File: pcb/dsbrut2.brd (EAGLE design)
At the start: 100 x 80 mm, 11 parts, among them IC1 4175D, IC2 74HC125D, IC3 MEGA8-AI

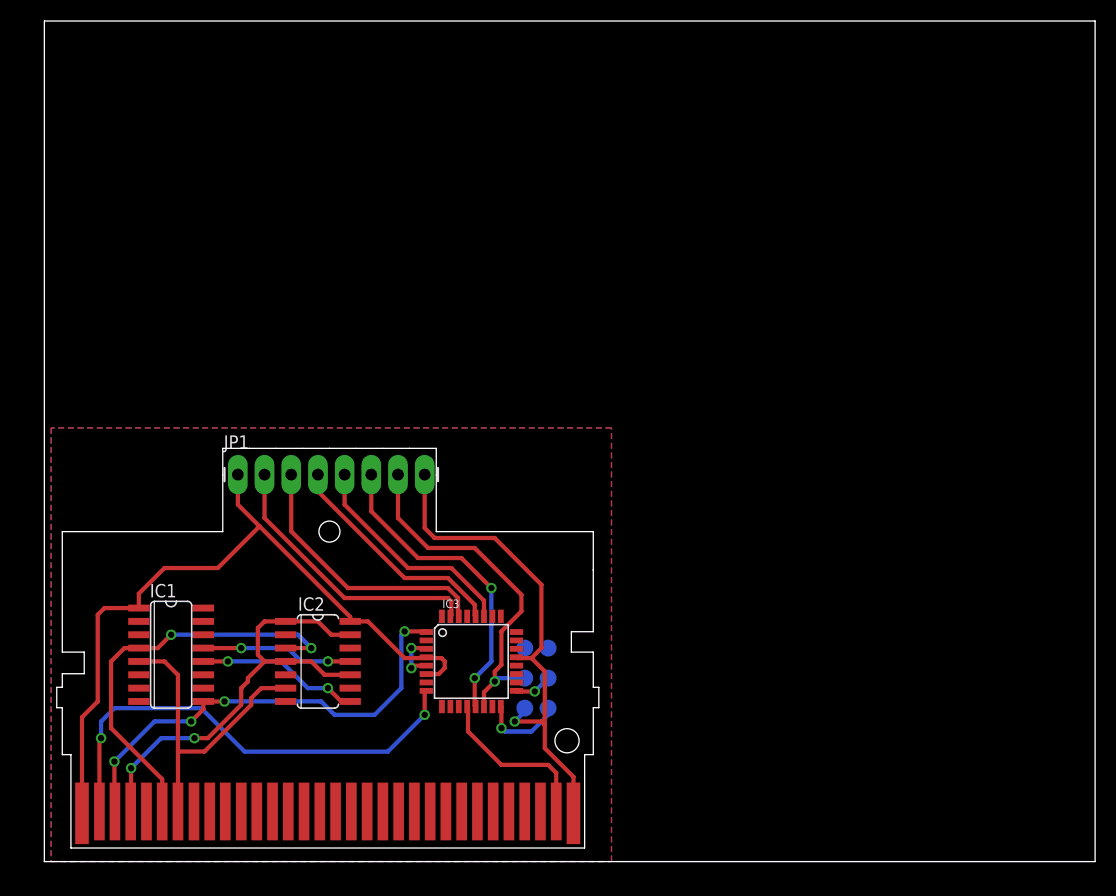
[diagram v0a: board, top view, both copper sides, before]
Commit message: updated isp progheader - please verify orientation
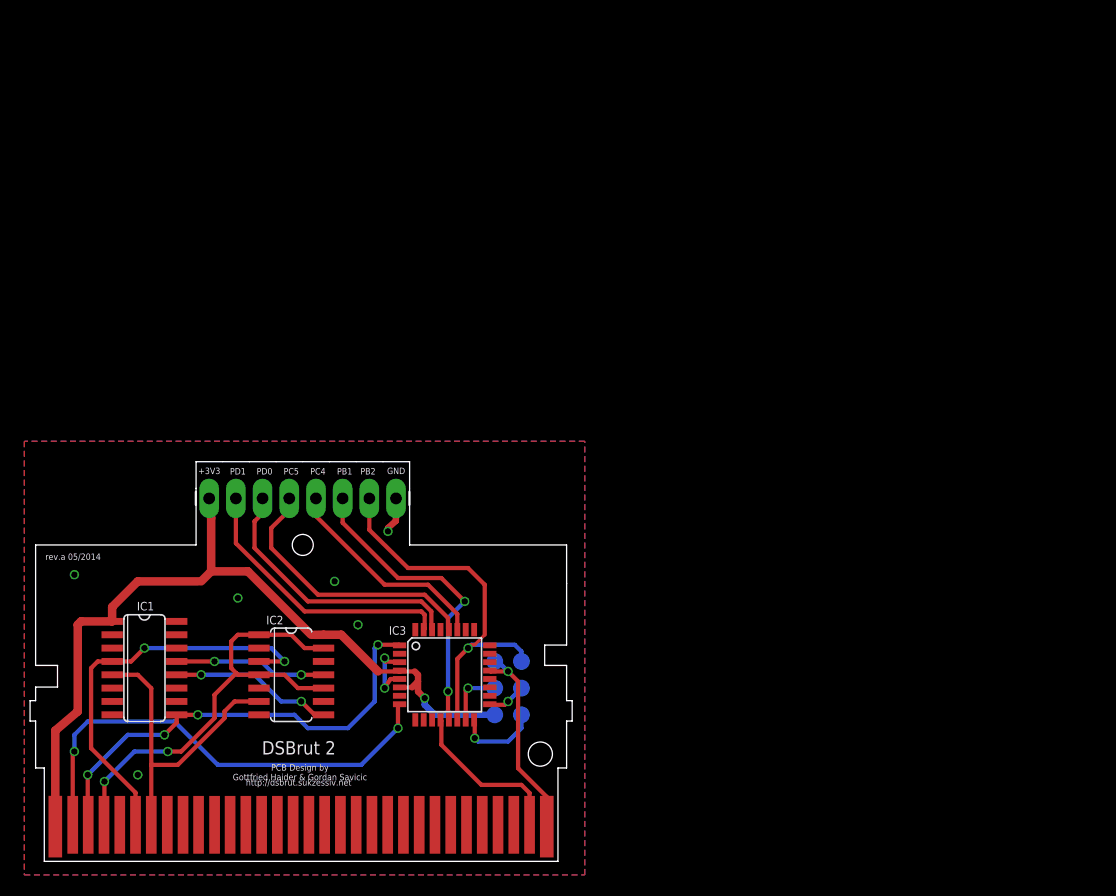
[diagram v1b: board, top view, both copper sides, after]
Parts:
- moved TP1 6.96 mm to (42.9, 14.0)
- moved TP2 6.35 mm to (42.9, 16.5)
- moved TP6 5.28 mm to (42.9, 19.1)
- moved JP1 3.54 mm to (15.7, 34.6)
- moved U$1 2.84 mm to (0.00, 0.00)
- moved IC1 2.84 mm to (9.53, 18.4)
- moved IC2 2.84 mm to (23.5, 17.8)
- moved IC3 2.84 mm to (38.1, 17.8)
- moved TP4 2.71 mm to (45.4, 16.5)
- moved TP3 2.62 mm to (45.4, 14.0)
- moved TP5 1.62 mm to (45.4, 19.1)
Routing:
- net GND: track 53.2 -> 29.6 mm, vias 3 -> 9
- net +3V3: track 70.9 -> 78.8 mm, vias 0 -> 1
- net MOSI: track 0.00 -> 5.65 mm, vias 0 -> 1
- net PC5: track 22.1 -> 26.2 mm
- net PB2: track 34.0 -> 36.7 mm
- net PB1: track 29.9 -> 29.0 mm
- net PC4: track 21.4 -> 20.5 mm
- net GBA6: track 39.4 -> 38.8 mm
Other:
- board size 100 x 80 mm -> 51.6 x 38 mm
- board text added: "+3V3"
- board text added: "DSBrut 2"
- board text added: "GND"
- board text added: "PB1"
- board text added: "PB2"
- board text added: "PC4"
- board text added: "PC5"
- board text added: "PCB Design by Gottfried Haider & Gordan Savicic"
- board text added: "PD0"
- board text added: "PD1"
- board text added: "http://dsbrut.sukzessiv.net"
- board text added: "rev.a 05/2014"

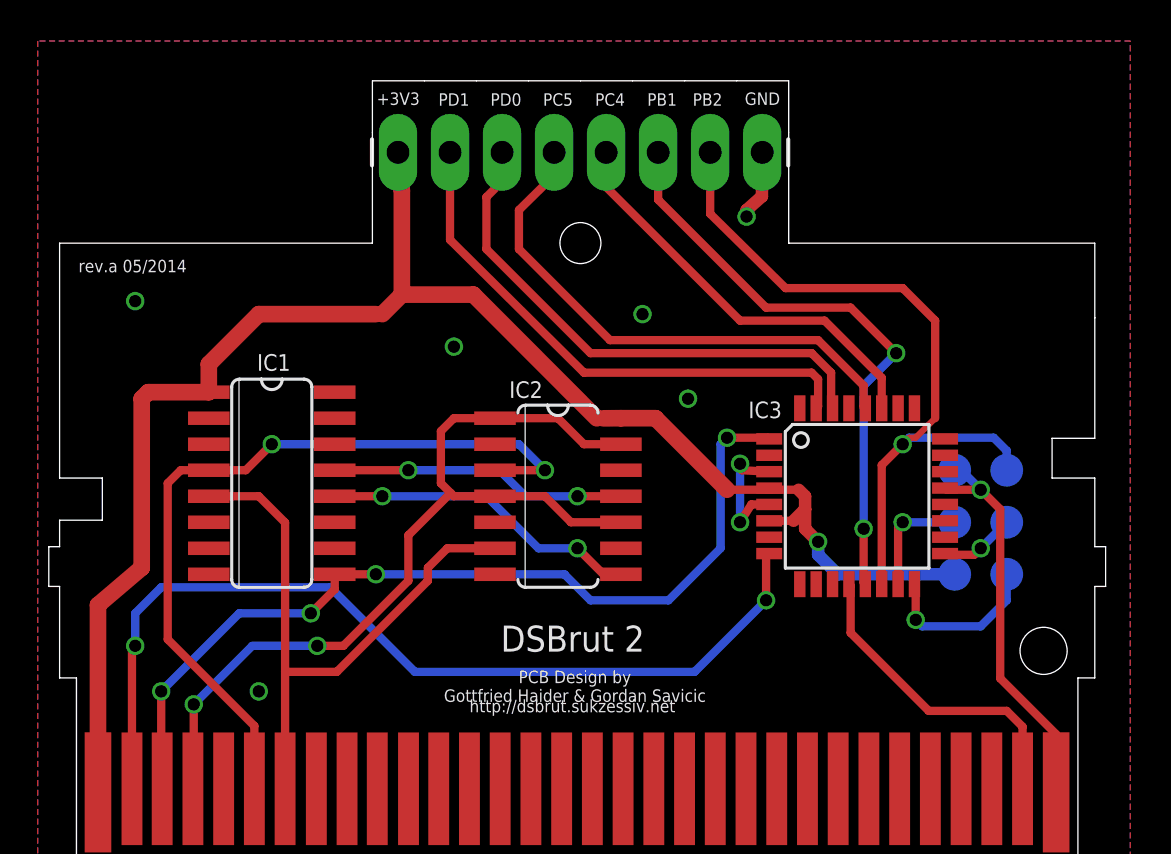
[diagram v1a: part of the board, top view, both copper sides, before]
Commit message: added rst, sck led, aref vcc, cleanup
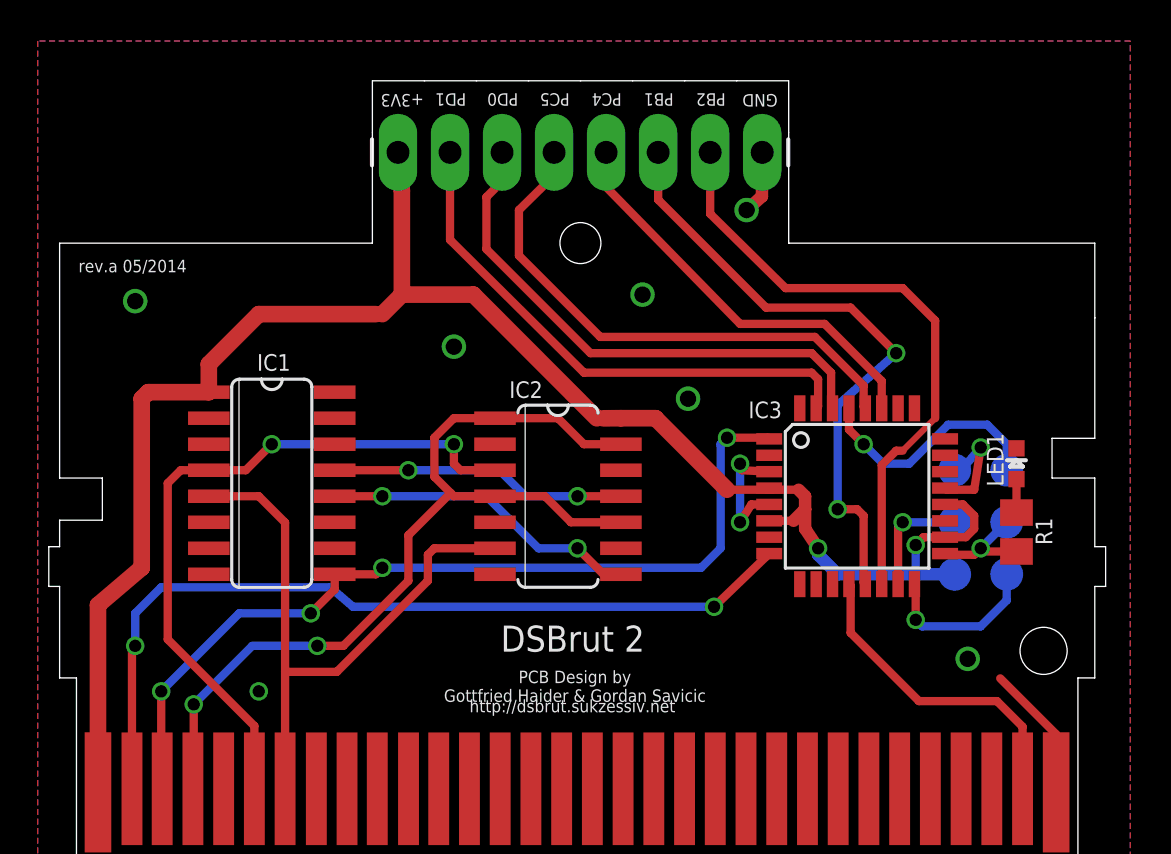
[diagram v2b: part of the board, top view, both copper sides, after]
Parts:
- added LED1: (no value), SparkFunEagle-6-6-07:LED-0603
- added R1: (no value), rcl:M0805
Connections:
- removed net AVCC: IC3.18
- new net N$4: LED1.A, R1.2
- new net RST: IC3.29, TP5.TP
- net +3V3: now also IC3.18, IC3.20
- net GND: now also LED1.C
- net PB2: no longer TP5.TP
- net SCK: now also R1.1
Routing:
- net RST: track 0.00 -> 11.9 mm, vias 0 -> 1
- net GND: track 29.6 -> 21.6 mm, vias 9 -> 10
- net +3V3: track 78.8 -> 85.7 mm, vias 1 -> 2
- net PB2: track 36.7 -> 30.3 mm, vias 1 -> 0
- net GBA6: track 38.8 -> 34.5 mm
- net GBA2: track 45.5 -> 41.5 mm
- net SCK: track 3.69 -> 5.64 mm
- net PB1: track 29.0 -> 30.7 mm
- net N$4: track 0.00 -> 1.63 mm
- net WR: track 44.1 -> 43.0 mm

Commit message: Add GBA{8,9} and connections between IC{1,2} and the AtMega
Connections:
- removed net GBA5: U$1.P$5
- net GBA8: now also U$1.P$8
- net GBA9: now also U$1.P$9
- net PC0: now also IC3.23
- net PC1: now also IC3.24
- net PC2: now also IC3.25
- net PC3: now also IC3.26
- net PD4: now also IC3.2
- net PD5: now also IC3.9
- net PD6: now also IC3.10
- net PD7: now also IC3.11
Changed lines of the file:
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@@
 <signal name="PD4">
 <contactref element="IC1" pad="2"/>
+<contactref element="IC3" pad="2"/>
+<wire x1="6.4516" y1="21.59" x2="33.8074" y2="19.78" width="0" layer="19" extent="1-1"/>
 </signal>
 <signal name="GBA6">
@@
 <signal name="PD5">
 <contactref element="IC1" pad="7"/>
+<contactref element="IC3" pad="9"/>
+<wire x1="6.4516" y1="15.24" x2="35.3" y2="13.4874" width="0" layer="19" extent="1-1"/>
 </signal>
 <signal name="WR">
@@
 <signal name="PD6">
 <contactref element="IC1" pad="10"/>
+<contactref element="IC3" pad="10"/>
+<wire x1="12.5984" y1="15.24" x2="36.1" y2="13.4874" width="0" layer="19" extent="1-1"/>
 </signal>
 <signal name="GBA8">
@@
 <via x="14.9225" y="17.78" extent="1-16" drill="0.6"/>
 <wire x1="14.9225" y1="17.78" x2="12.5984" y2="17.78" width="0.4064" layer="1"/>
+<contactref element="U$1" pad="P$8"/>
+<wire x1="11.7" y1="3.5" x2="12.5984" y2="17.78" width="0" layer="19" extent="1-1"/>
 </signal>
 <signal name="GBA9">
@@
 <via x="16.1925" y="19.05" extent="1-16" drill="0.6"/>
 <wire x1="16.1925" y1="19.05" x2="12.5984" y2="19.05" width="0.4064" layer="1"/>
+<contactref element="U$1" pad="P$9"/>
+<wire x1="13.2" y1="3.5" x2="12.5984" y2="19.05" width="0" layer="19" extent="1-1"/>
 </signal>
 <signal name="PD7">
 <contactref element="IC1" pad="15"/>
+<contactref element="IC3" pad="11"/>
+<wire x1="12.5984" y1="21.59" x2="36.9" y2="13.4874" width="0" layer="19" extent="1-1"/>
 </signal>
 <signal name="PC3">
 <contactref element="IC2" pad="12"/>
+<contactref element="IC3" pad="26"/>
+<wire x1="26.5684" y1="19.05" x2="40.1" y2="22.0726" width="0" layer="19" extent="1-1"/>
 </signal>
 <signal name="PC1">
 <contactref element="IC2" pad="5"/>
+<contactref element="IC3" pad="24"/>
+<wire x1="20.4216" y1="16.51" x2="42.3926" y2="20.58" width="0" layer="19" extent="1-1"/>
 </signal>
 <signal name="PC0">
 <contactref element="IC2" pad="2"/>
+<contactref element="IC3" pad="23"/>
+<wire x1="20.4216" y1="20.32" x2="42.3926" y2="19.78" width="0" layer="19" extent="1-1"/>
 </signal>
 <signal name="RD">
@@
 <signal name="PC2">
 <contactref element="IC2" pad="9"/>
+<contactref element="IC3" pad="25"/>
+<wire x1="26.5684" y1="15.24" x2="40.9" y2="22.0726" width="0" layer="19" extent="1-1"/>
 </signal>
 <signal name="GBA31">
@@
 <wire x1="33.655" y1="14.8276" x2="33.8074" y2="14.98" width="0.4064" layer="1"/>
 </signal>
-<signal name="GBA5">
-<contactref element="U$1" pad="P$5"/>
-</signal>
 <signal name="MOSI">

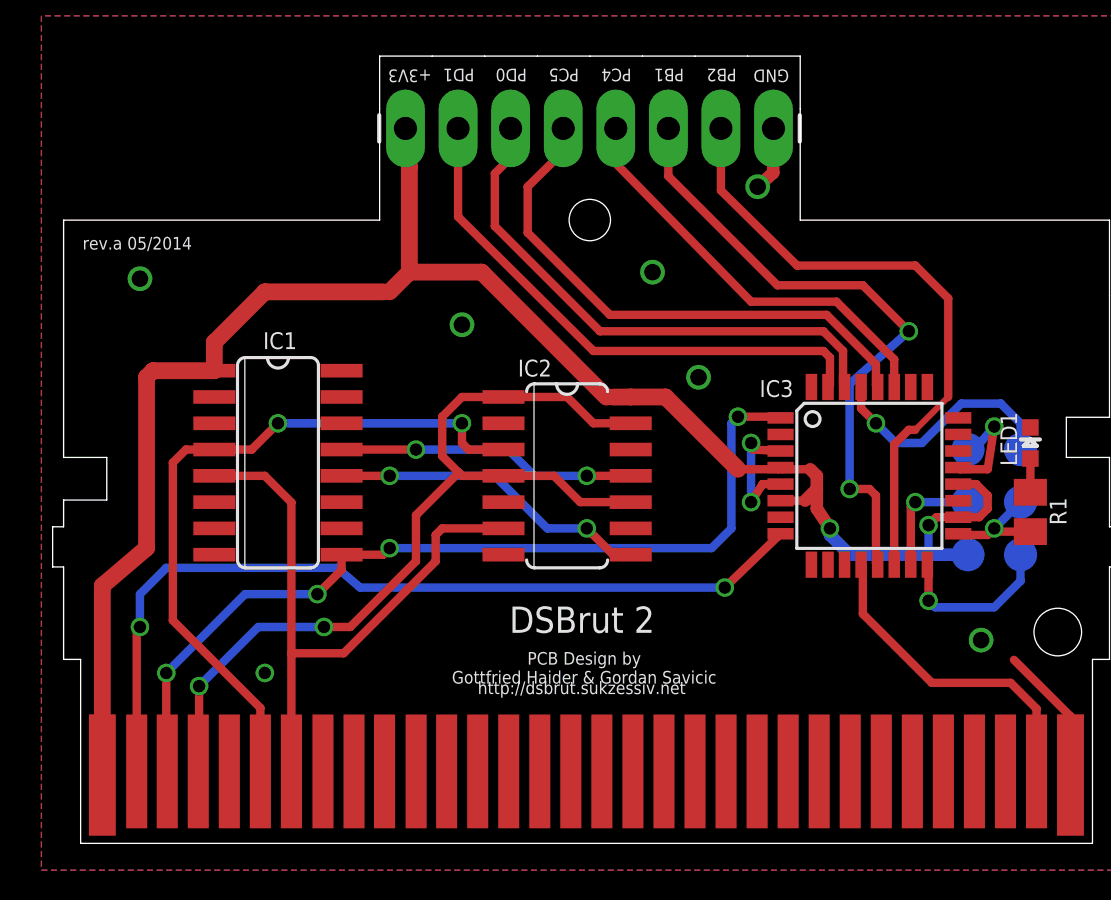
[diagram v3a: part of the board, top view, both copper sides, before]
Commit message: from 2to4to2 layers - added gba4/5/6/7/8 etc...
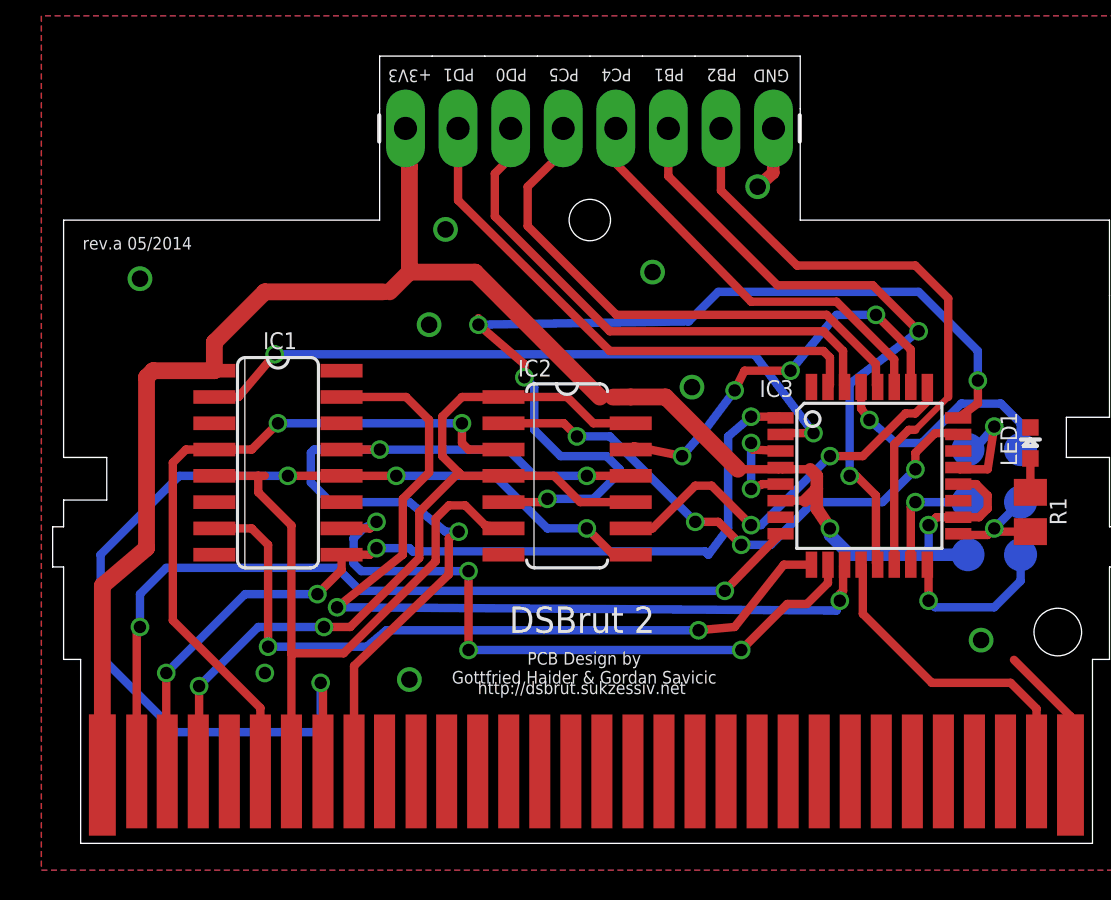
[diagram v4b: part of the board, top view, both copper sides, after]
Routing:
- net PC1: track 0.00 -> 47.5 mm, vias 0 -> 4
- net PD7: track 0.00 -> 42.3 mm, vias 0 -> 2
- net GBA8: track 15.5 -> 52.4 mm, vias 2 -> 4
- net PD5: track 0.00 -> 35.9 mm, vias 0 -> 2
- net PD6: track 0.00 -> 33.5 mm, vias 0 -> 4
- net PD4: track 0.00 -> 33.4 mm, vias 0 -> 2
- net PC0: track 0.00 -> 27.1 mm, vias 0 -> 4
- net GBA9: track 14.5 -> 41.2 mm, vias 2 -> 3
- net PC3: track 0.00 -> 19.5 mm, vias 0 -> 4
- net PC2: track 0.00 -> 19.2 mm, vias 0 -> 2
- net GBA7: track 30.7 -> 32.2 mm
- net GND: track 21.6 -> 20.5 mm, vias 10 -> 12

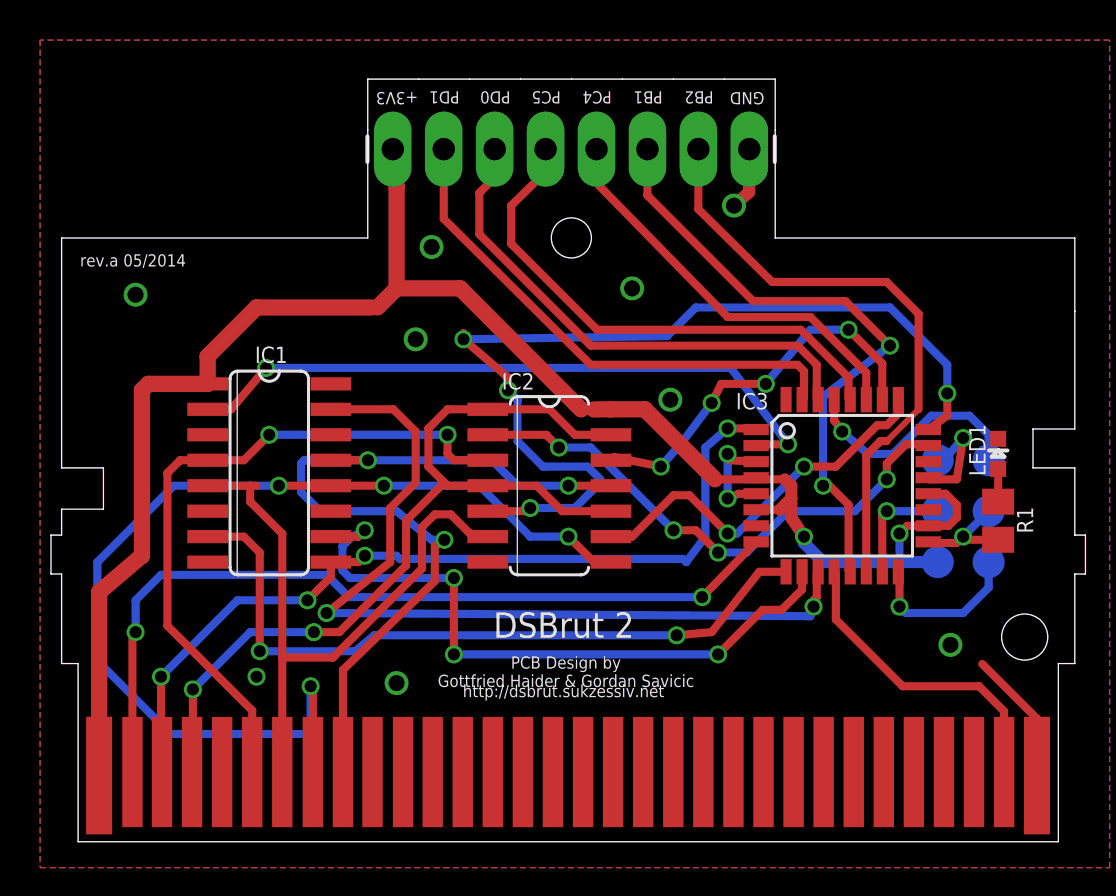
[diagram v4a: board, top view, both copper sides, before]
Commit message: Connected RD to ATmega, added TX/RX labels, removed ground plane underneath Slot -2 pins
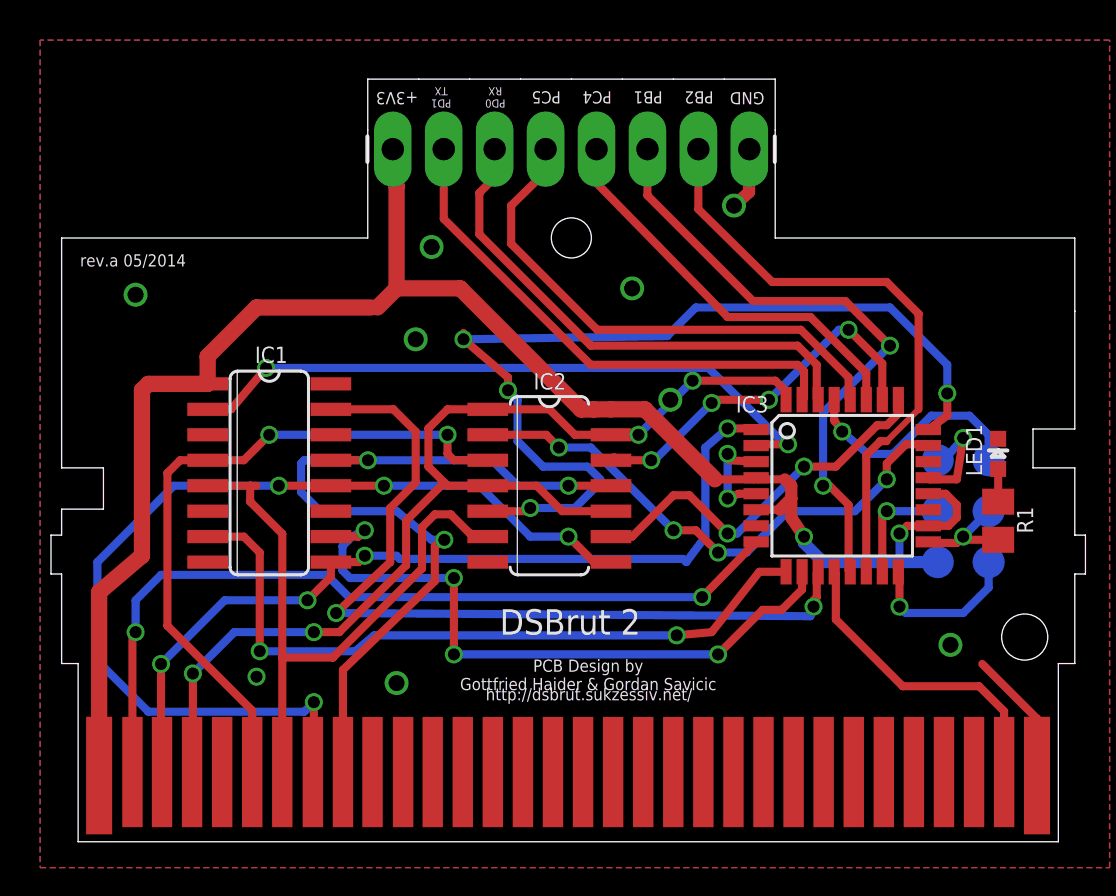
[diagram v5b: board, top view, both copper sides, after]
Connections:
- net RD: now also IC3.32
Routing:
- net RD: track 44.2 -> 55.2 mm, vias 2 -> 4
- net GBA8: track 52.4 -> 49.2 mm
- net PD7: track 42.3 -> 41.4 mm
- net PC3: track 19.5 -> 19.0 mm
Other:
- board text added: "PD0 RX"
- board text added: "PD1 TX"
- board text added: "http://dsbrut.sukzessiv.net/"
- board text removed: "PD0"
- board text removed: "PD1"
- board text removed: "http://dsbrut.sukzessiv.net"
